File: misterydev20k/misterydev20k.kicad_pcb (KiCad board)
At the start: 2 copper layers, 90 x 67 mm, 184 parts, among them J1 SWD, J11 Joystick 0, J12 Joystick 1, J13 USB_A_Stacked, J2 USB_C_Receptacle_USB2.0, J3 Jumper block, J4 Micro_SD_Card_Det1, J5 HDMI_A, J6 Grove 1125S-4P, J7 USB_A_Stacked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

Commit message: Small board cleanups
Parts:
- added R58: 4k7, Resistor_SMD:R_0402_1005Metric, F.Cu at (130.2, 84.0)
- moved C58 0.96 mm to (113.4, 82.2)
- moved C48 0.35 mm to (140.2, 62.8)
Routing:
- net GND: track 269.9 -> 310.2 mm, vias 64 -> 81
- net +3V3: track 446.1 -> 456.2 mm, vias 31 -> 32
- net Net-(RN3-R4.1): track 27.8 -> 30.0 mm
- net Net-(RN1-R1.1): track 29.9 -> 32.0 mm
- net Net-(RN1-R2.1): track 30.0 -> 32.2 mm
- net MON_RX: track 36.0 -> 34.1 mm
- net SPARE: track 63.1 -> 61.2 mm
- net MON_TX: track 30.2 -> 28.5 mm
- net JOYB3: track 48.9 -> 50.6 mm
- net SWCLK: track 18.0 -> 19.6 mm
- net Net-(RN3-R3.1): track 27.9 -> 29.5 mm
- net DBG TX: track 75.0 -> 73.4 mm
- net HR_IO3: track 56.8 -> 55.4 mm
- net MISO: track 76.6 -> 75.2 mm
- net MOSI: track 76.1 -> 74.8 mm
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
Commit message: More small pcb updates
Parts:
- added C62: 100nF, Capacitor_SMD:C_0402_1005Metric, F.Cu at (128.0, 75.4)
- added C63: 100nF, Capacitor_SMD:C_0402_1005Metric, F.Cu at (129.0, 61.8)
- added C64: 100nF, Capacitor_SMD:C_0402_1005Metric, F.Cu at (140.8, 75.2)
- added C65: 100nF, Capacitor_SMD:C_0603_1608Metric, B.Cu at (135.6, 63.4)
- added C66: 100nF, Capacitor_SMD:C_0603_1608Metric, B.Cu at (141.0, 72.0)
- added C67: 100nF, Capacitor_SMD:C_0603_1608Metric, B.Cu at (129.6, 72.2)
- added C68: 100nF, Capacitor_SMD:C_0603_1608Metric, B.Cu at (129.6, 66.0)
- moved C50 0.99 mm to (141.8, 75.2)
- moved FB3 0.61 mm to (130.3, 60.2)
- moved R52 0.43 mm to (144.2, 66.4)
- moved C49 0.10 mm to (139.4, 75.2)
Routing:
- net GND: track 310.2 -> 342.8 mm, vias 81 -> 89
- net HR_CLK: track 24.7 -> 26.4 mm
- net +1V0: track 64.3 -> 65.8 mm
- net +3V3: track 456.2 -> 457.3 mm
- net MISO: track 75.2 -> 76.2 mm
- net SD_DAT0: track 43.9 -> 43.0 mm
- net JOYA2: track 49.1 -> 48.2 mm
- net MOSI: track 74.8 -> 75.5 mm
- net VCCPLLL: track 6.89 -> 7.50 mm
- net SD_DAT1: track 29.2 -> 28.6 mm

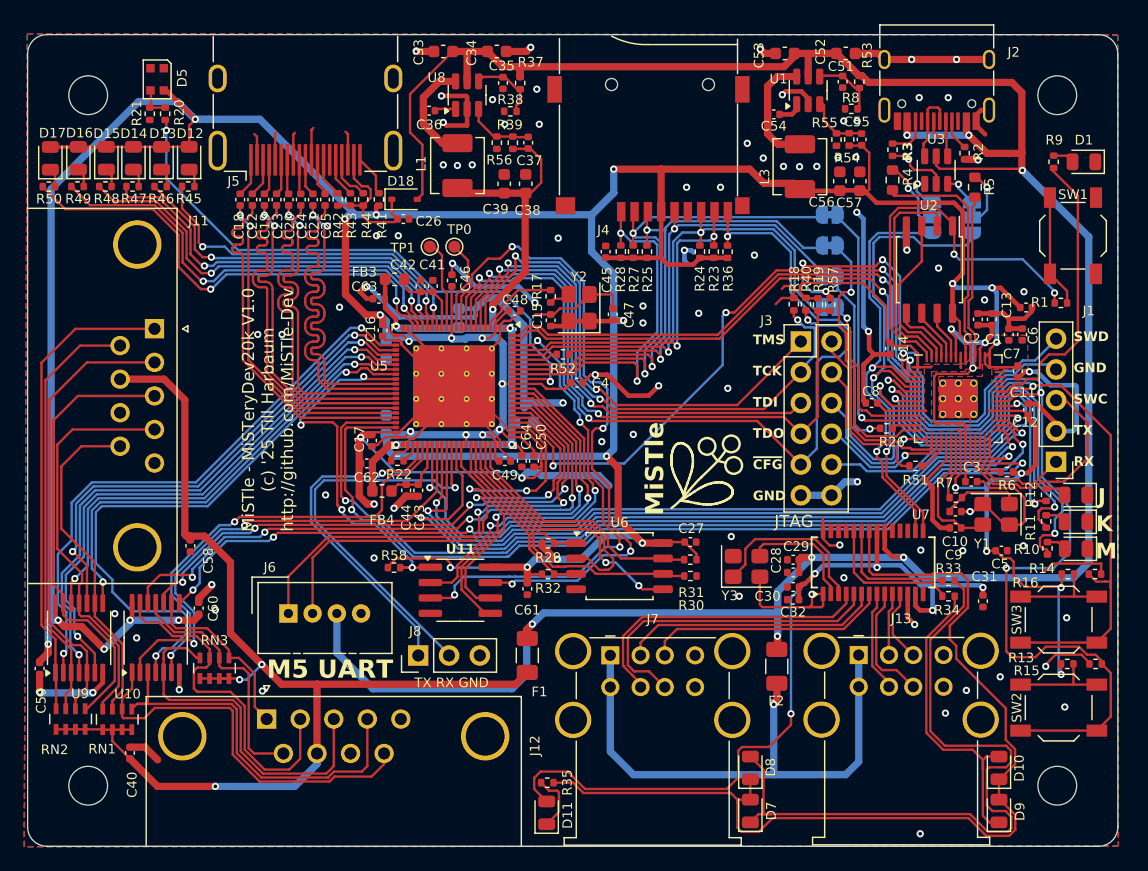
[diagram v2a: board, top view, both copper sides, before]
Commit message: Fix FPGA orientation in production files
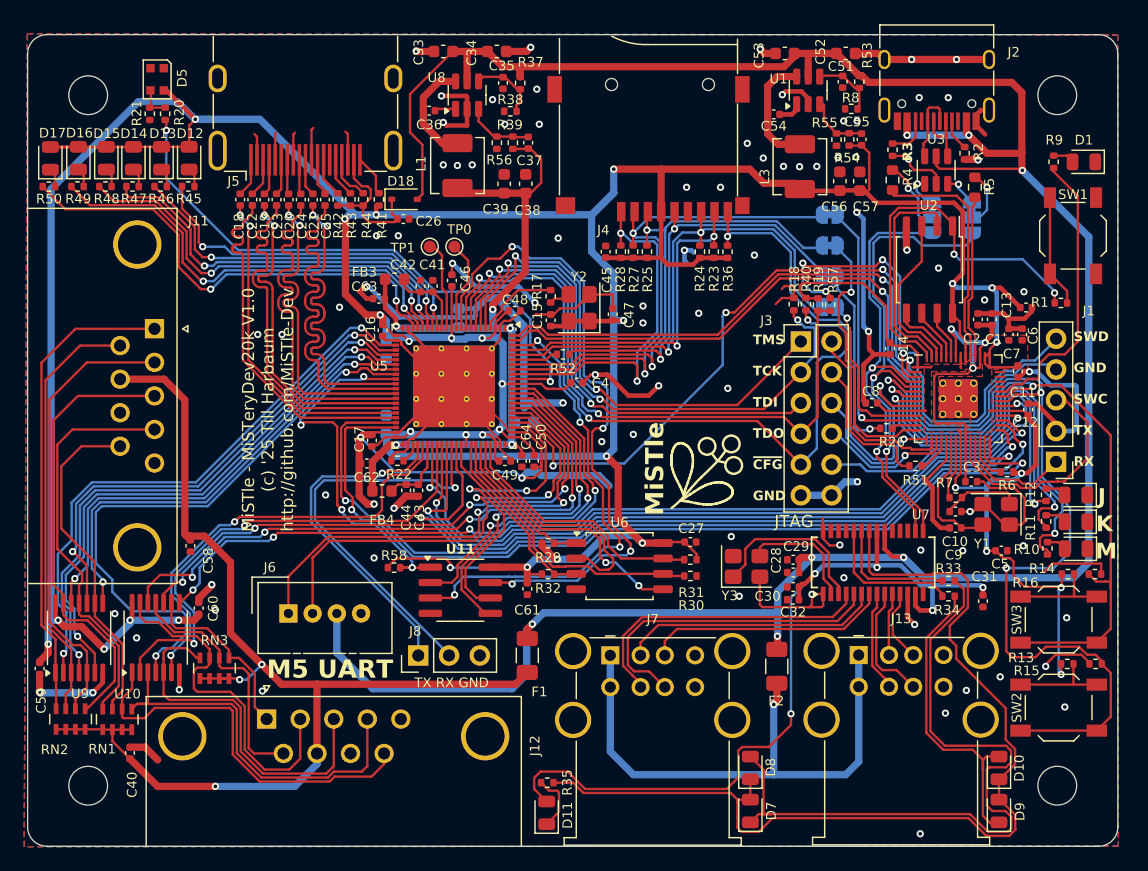
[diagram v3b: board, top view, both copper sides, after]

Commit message: Replace ch334u by ch334r due to availablity
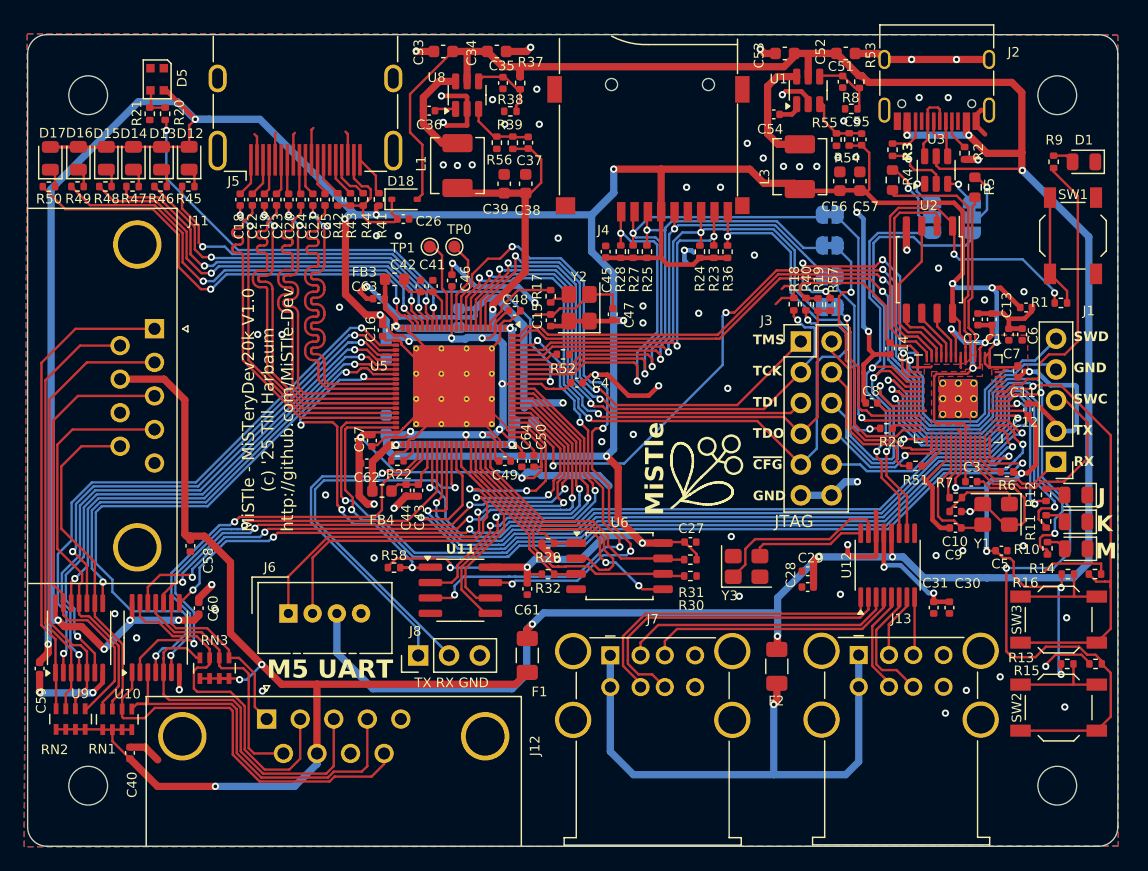
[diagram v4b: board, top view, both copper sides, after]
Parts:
- removed C32: 1uF, Capacitor_SMD:C_0402_1005Metric
- removed D10: PORT1, LED_SMD:LED_0805_2012Metric
- removed D11: ACTIVE, LED_SMD:LED_0805_2012Metric
- removed D7: PORT4, LED_SMD:LED_0805_2012Metric
- removed D8: PORT3, LED_SMD:LED_0805_2012Metric
- removed D9: PORT2, LED_SMD:LED_0805_2012Metric
- removed R33, R34: 220, Resistor_SMD:R_0402_1005Metric
- removed R35: 470, Resistor_SMD:R_0402_1005Metric
- removed U7: CH334U, Package_SO:SSOP-28_3.9x9.9mm_P0.635mm
- added U12: CH334R, Package_SO:QSOP-16_3.9x4.9mm_P0.635mm, F.Cu at (171.0, 83.8)
- moved C30 13.0 mm to (176.1, 87.3), turned to 90 degrees
- moved C31 4.10 mm to (174.8, 87.3)
- moved C28 1.70 mm to (164.4, 85.6)
- moved C29 1.53 mm to (164.4, 84.3)
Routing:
- net USB LED 4: track 81.7 -> 0.00 mm
- net Net-(D7-K): track 59.1 -> 0.00 mm
- net Net-(U12-VDD33_{LDO}): track 67.5 -> 9.94 mm, vias 5 -> 2
- net Net-(D10-A): track 26.2 -> 0.00 mm
- net USB LED 2: track 11.7 -> 0.00 mm
- net USB LED 1: track 10.4 -> 0.00 mm
- net GND: track 342.8 -> 332.8 mm, vias 89 -> 86
- net Net-(D11-K): track 4.85 -> 0.00 mm
- net /USB Hub/USB4_D-: track 25.1 -> 26.5 mm
- net +5V: track 217.9 -> 216.6 mm
- net /USB Hub/USB1_D+: track 6.00 -> 4.82 mm
- net /USB Hub/USB3_D-: track 21.5 -> 22.6 mm
- net /USB Hub/USB3_D+: track 20.1 -> 21.3 mm
- net /USB Hub/USB4_D+: track 26.8 -> 27.9 mm
- net Net-(U12-XO): track 14.1 -> 14.9 mm

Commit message: Update misterydev20k to v1.1
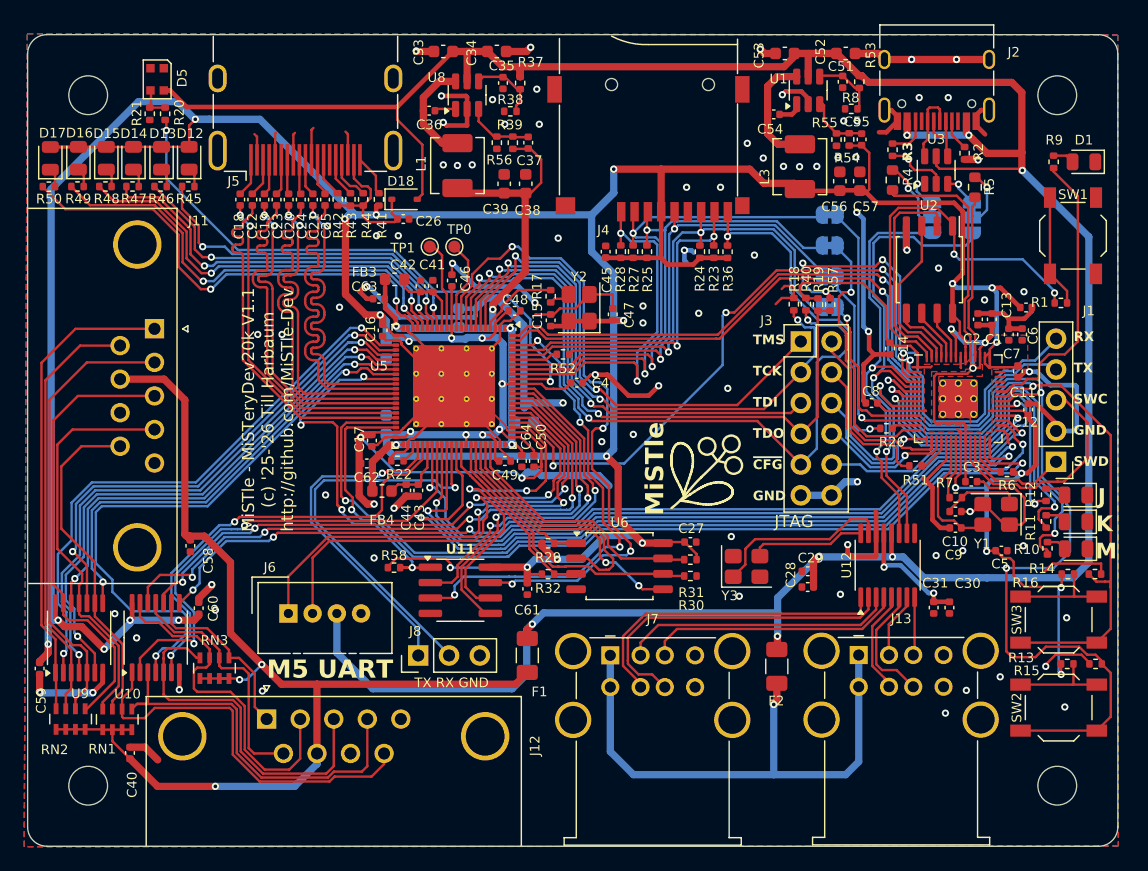
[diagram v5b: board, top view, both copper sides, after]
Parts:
- U2: value W25Q128JVS -> W25Q64VS
- U6: value W25Q128JVS -> W25Q64JVS
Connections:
- D5 pad 4: +3V3 -> +5V
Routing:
- net +5V: track 216.6 -> 243.8 mm
- net GND: track 332.8 -> 336.4 mm
- net +3V3: track 457.3 -> 453.7 mm
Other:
- board text added: "MiSTle - MiSTeryDev20k V1.1 (c) '25-'26 Till Harbaum http://github.com/MiSTle-Dev"
- board text added: "RX TX SWC GND SWD"
- board text removed: "MiSTle - MiSTeryDev20k V1.0 (c) '25 Till Harbaum http://github.com/MiSTle-Dev"
- board text removed: "SWD GND SWC TX RX"
